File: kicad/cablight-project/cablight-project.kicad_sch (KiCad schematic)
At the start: 16 parts, among them J1 Screw_Term_1x2_2.54mm, J2 Screw_Term_1x2_2.54mm, P1 Pololu D24V10F5, Q1 IRLB8721PBF, SW1 PEC11, SW3 switch_SPDT_SLW_121586

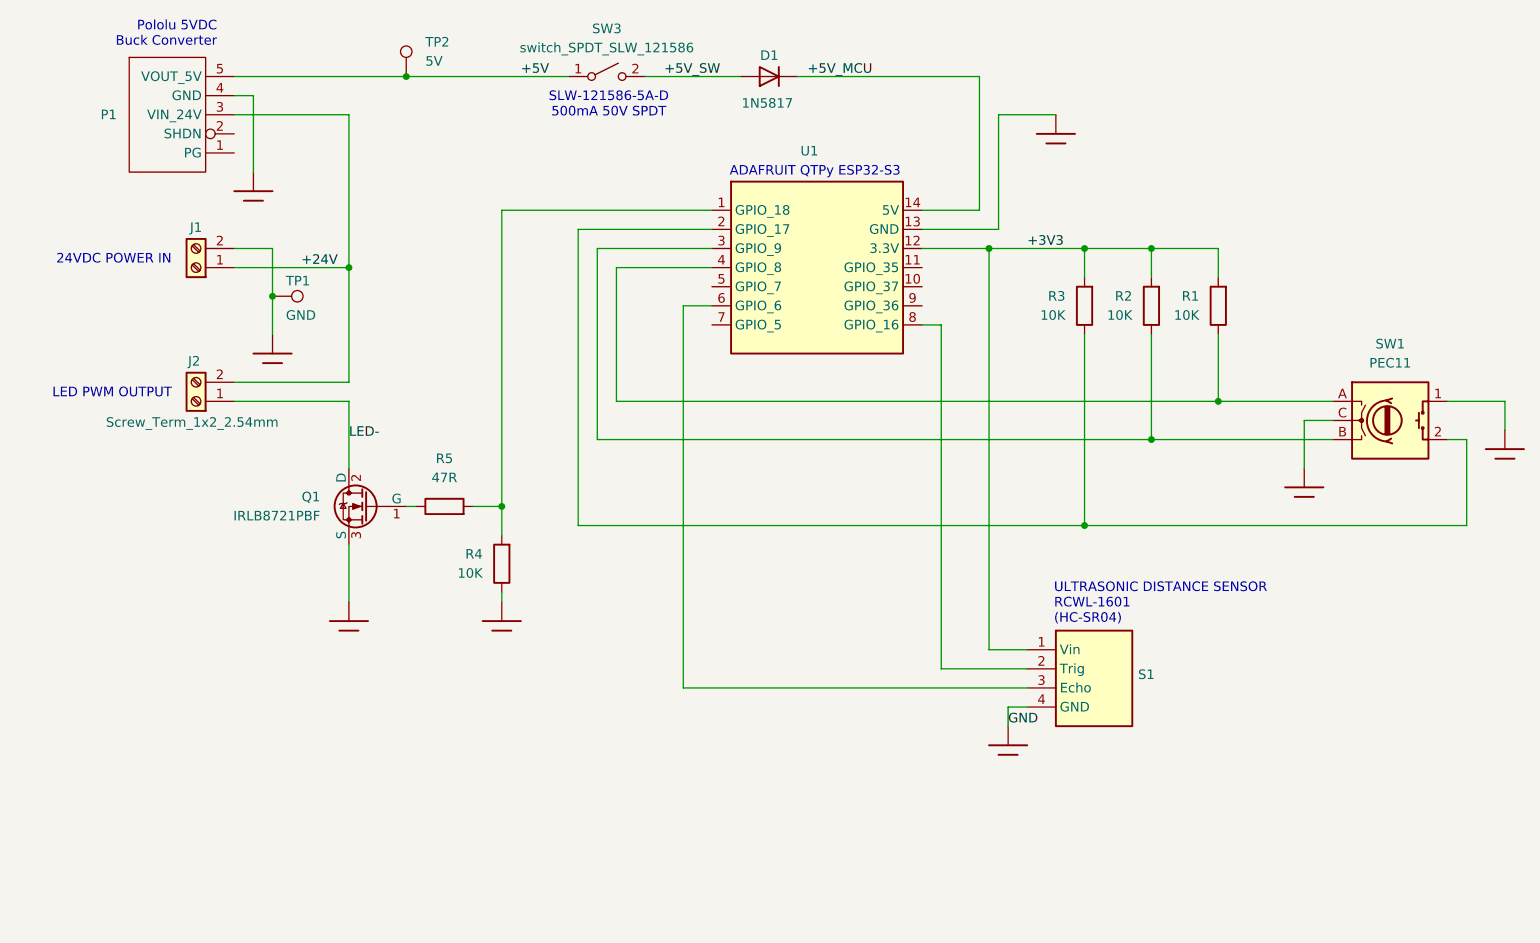
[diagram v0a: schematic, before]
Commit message: Add Button code support and make ultrasonic notify from task.
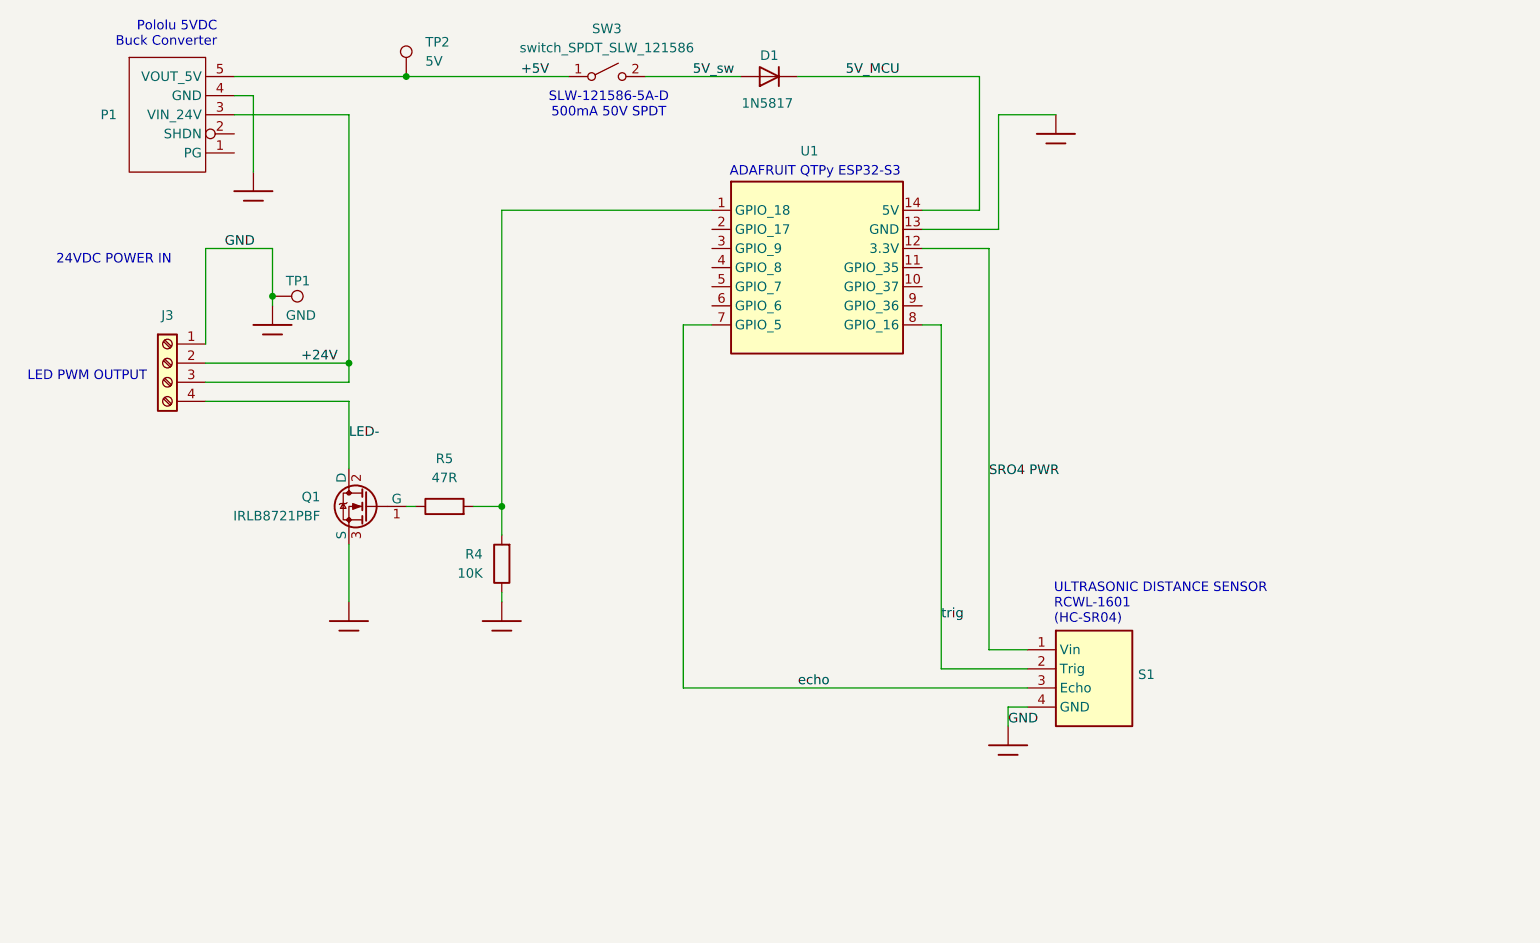
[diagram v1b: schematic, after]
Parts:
- removed J1, J2: Screw_Term_1x2_2.54mm, user:2xTermBlock_254mm, symbol user:Screw_Term_1x2_2.54mm
- removed R1, R2, R3: 10K, Resistor_THT:R_Axial_DIN0207_L6.3mm_D2.5mm_P10.16mm_Horizontal, symbol user:R
- removed SW1: PEC11, user:Bourns-PEC11R, symbol Device:RotaryEncoder_Switch
- added J3: Screw_Term_1x4_5mm, Library:Molex 4pin Terminal Block, symbol extra:Screw_Term_1x4_5mm
- R4, R5: footprint Resistor_THT:R_Axial_DIN0207_L6.3mm_D2.5mm_P10.16mm_Horizontal -> Resistor_THT:R_Axial_DIN0207_L6.3mm_D2.5mm_P9.5mm
- TP1, TP2: footprint TestPoint:TestPoint_Plated_Hole_D2.0mm -> TestPoint:TestPoint_THTPad_D1.0mm_Drill0.5mm
- U1: footprint user:AdafruitQTPyEsp32S3 -> GRK_Lib:AdafruitQTPyEsp32S3; symbol user:Adafruit_QTPy_Esp32S3 -> GRK_Global_Sym_Lib:Adafruit_QTPy_Esp32S3
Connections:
- net +24V: now also J3.2 (Pin_2), J3.3 (Pin_3)
- net GND: now also TP1.1, J3.1 (Pin_1)
- net LED-: now also J3.4 (Pin_4)
- net at U1.6 (GPIO_6): no longer S1.3 (Echo)
- net echo: now reaches U1.7 (GPIO_5)
- net echo: now also S1.3 (Echo)
- net trig: now reaches S1.2 (Trig), U1.8 (GPIO_16)
- net +3V3 renamed SRO4 PWR
- net +5V_MCU renamed 5V_MCU
- net +5V_SW renamed 5V_sw

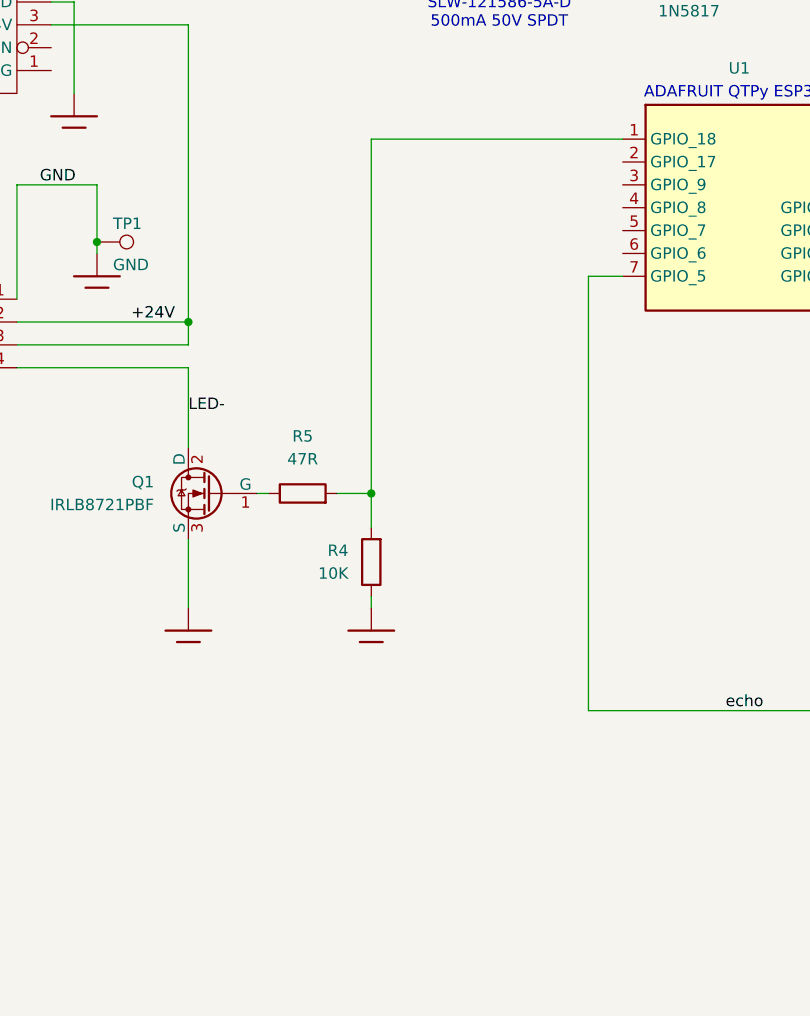
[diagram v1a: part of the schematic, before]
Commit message: add DIP switch to kicad
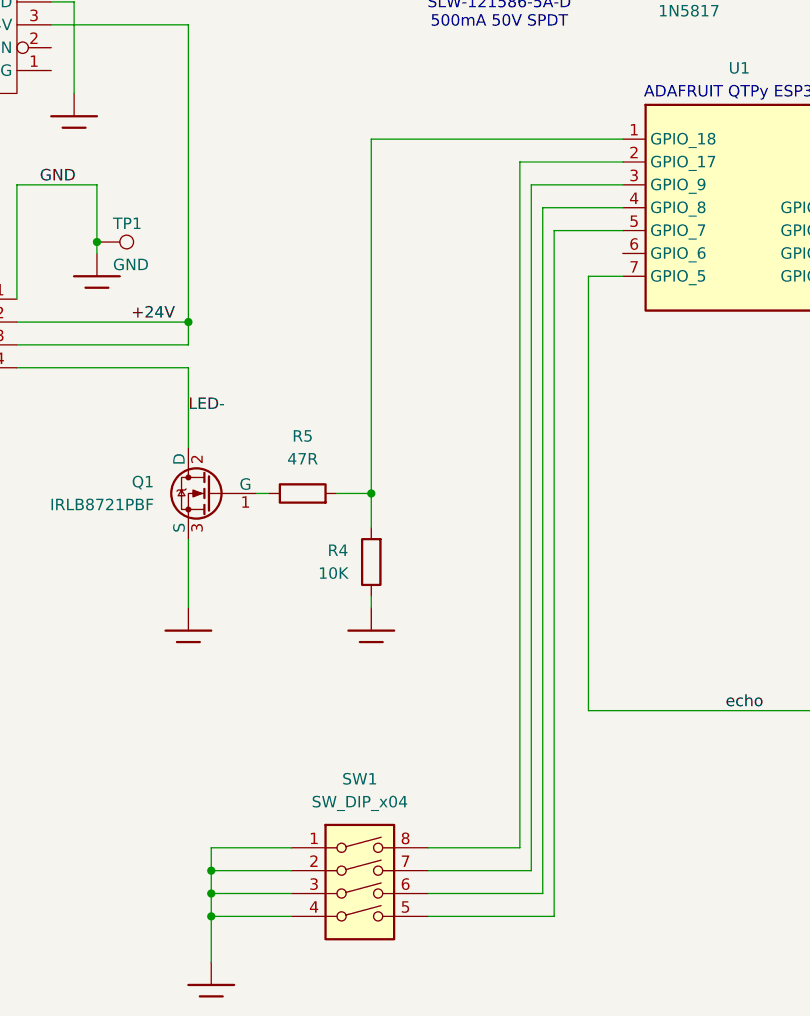
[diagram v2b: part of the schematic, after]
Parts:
- added SW1: SW_DIP_x04, GRK_Lib:DIP-4 DS04-254 SAME SKY, symbol Switch:SW_DIP_x04
- J3: footprint Library:Molex 4pin Terminal Block -> GRK_Lib:Molex 4pin Terminal Block
- P1: footprint user:Pololu_5V_H -> GRK_Lib:Pololu_5V_H
- Q1: footprint user:TO-220F-3_H_Heatsink -> GRK_Lib:TO-220F-3_H_Heatsink
- S1: footprint user:RCWL-1601 -> GRK_Lib:RCWL-1601
- SW3: footprint user:CUI_SPDT_500mA_3mm -> GRK_Lib:Switch_SPDT_CUI_500mA_3mm
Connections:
- net at U1.2 (GPIO_17): now also SW1.8
- net at U1.3 (GPIO_9): now also SW1.7
- net at U1.4 (GPIO_8): now also SW1.6
- net at U1.5 (GPIO_7): now also SW1.5
- new net: SW1.1, SW1.2, SW1.3, SW1.4

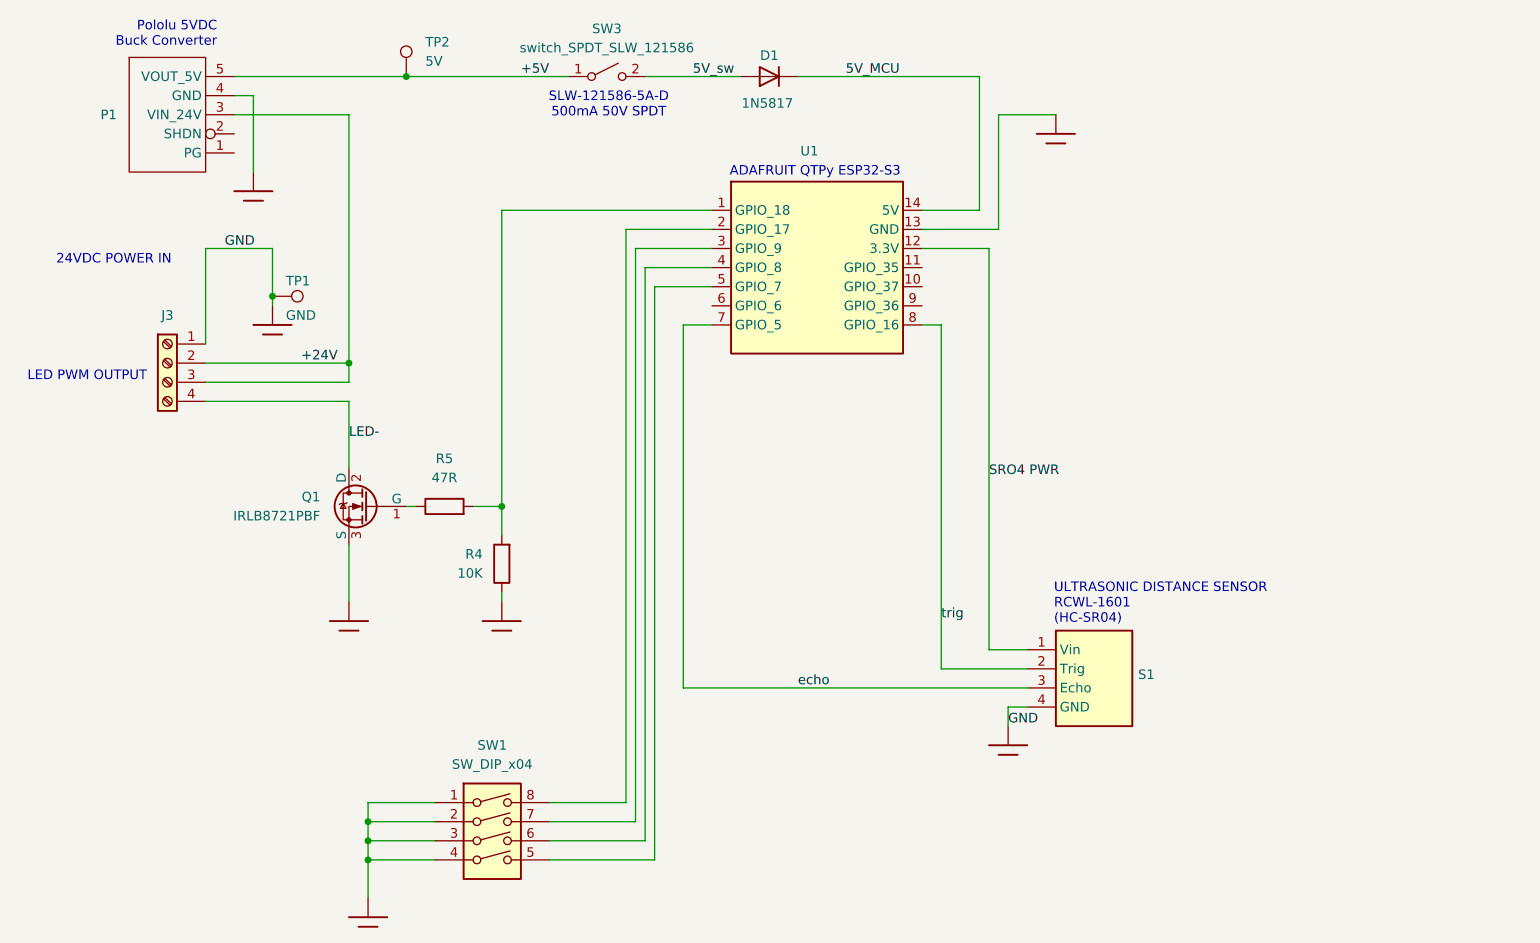
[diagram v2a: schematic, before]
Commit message: Layout KiCAD for DIP switches and button.
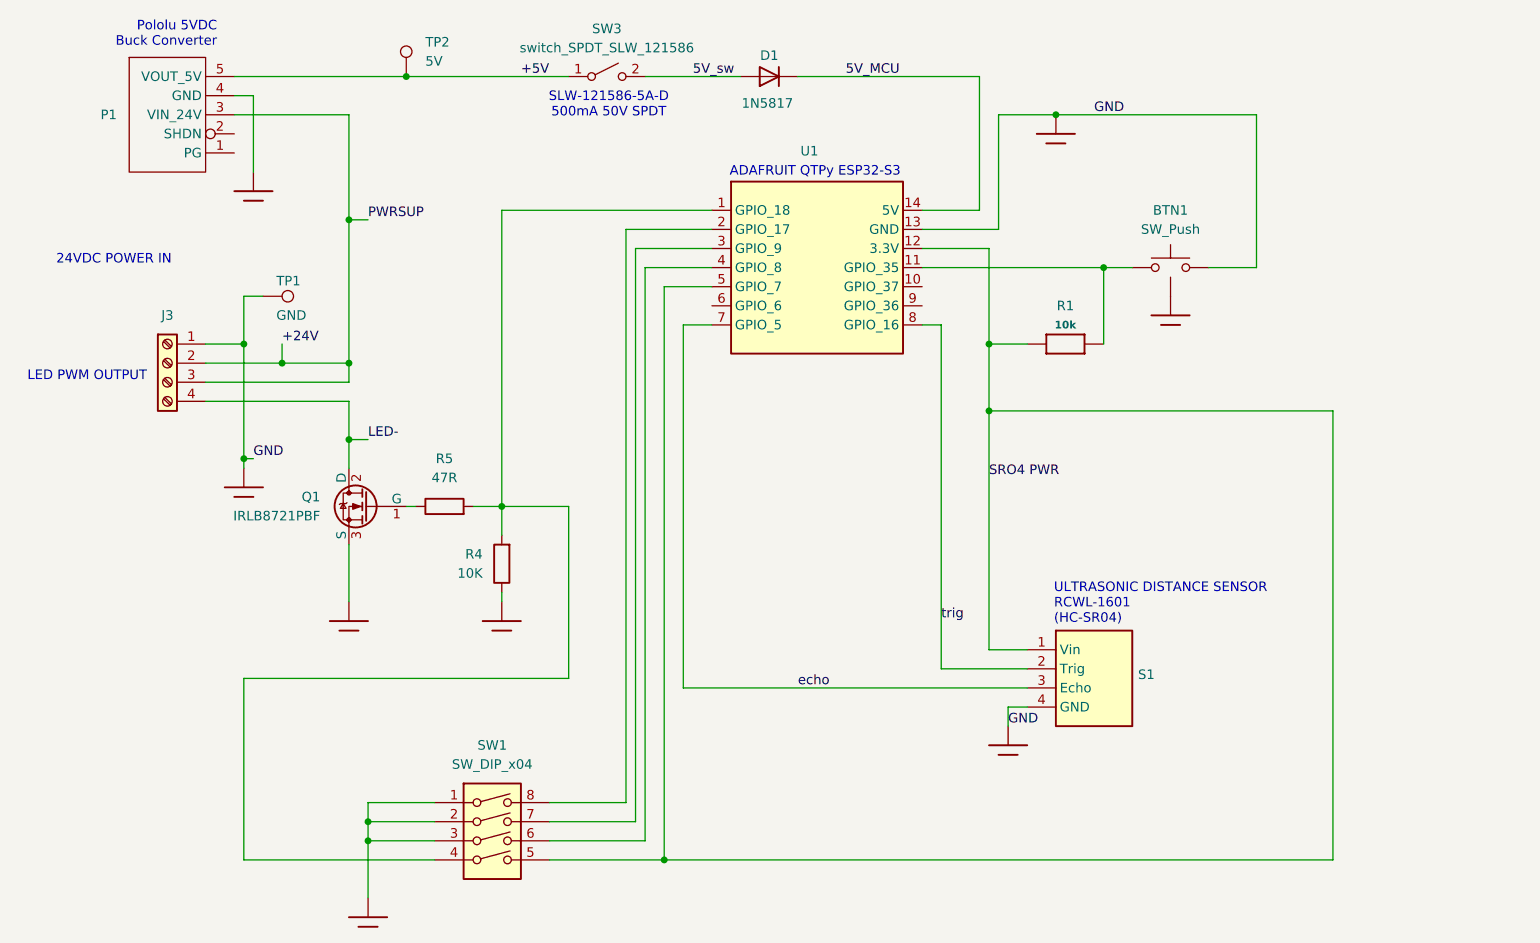
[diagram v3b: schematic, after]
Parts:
- added BTN1: SW_Push, GRK_Lib:Tactile Switch Wurth, symbol GRK_Global_Sym_Lib:SW_Push_With_GND
- added R1: 10k, Resistor_SMD:R_0805_2012Metric_Pad1.20x1.40mm_HandSolder, symbol cablight-eagle-import:RESISTOR_0805
- R4, R5: footprint Resistor_THT:R_Axial_DIN0207_L6.3mm_D2.5mm_P9.5mm -> Resistor_SMD:R_0805_2012Metric_Pad1.20x1.40mm_HandSolder
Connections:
- net GND: now also U1.13 (GND), BTN1.2
- net SRO4 PWR: now also SW1.5, U1.5 (GPIO_7), R1.1
- net at R4.1, R5.1, U1.1 (GPIO_18): now also SW1.4
- net at U1.11 (GPIO_35): now also BTN1.1, R1.2
- net at SW1.1, SW1.2, SW1.3: no longer SW1.4
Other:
- moved on the sheet: TP1

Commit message: progress
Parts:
- S1: footprint GRK_Lib:RCWL-1601 -> GRK_Lib:Molex 4pin Terminal Block 2.54mm
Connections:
- net at U1.10 (GPIO_37): now also U1.6 (GPIO_6), U1.9 (GPIO_36)
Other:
- note added: "Grounding all un-used pins."
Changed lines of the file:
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@@
+		)
+	)
+	(text "Grounding all\nun-used pins."
+		(exclude_from_sim no)
+		(at 131.064 101.092 0)
+		(effects
+			(font
+				(size 1.27 1.27)
+			)
 		)
 	)
@@
 	)
 	(junction
+		(at 149.86 77.47)
+		(diameter 0)
+		(color 0 0 0 0)
+	)
+	(junction
 		(at 162.56 52.07)
 		(diameter 0)
@@
 	)
 	(junction
+		(at 130.81 92.71)
+		(diameter 0)
+		(color 0 0 0 0)
+	)
+	(junction
 		(at 153.67 82.55)
 		(diameter 0)
@@
 	(wire
 		(pts
+			(xy 149.86 77.47) (xy 149.86 92.71)
+		)
+		(stroke
+			(width 0)
+			(type default)
+		)
+	)
+	(wire
+		(pts
+			(xy 149.86 74.93) (xy 149.86 77.47)
+		)
+		(stroke
+			(width 0)
+			(type default)
+		)
+	)
+	(wire
+		(pts
 			(xy 54.61 76.2) (xy 57.15 76.2)
 		)
@@
 	(wire
 		(pts
+			(xy 149.86 92.71) (xy 130.81 92.71)
+		)
+		(stroke
+			(width 0)
+			(type default)
+		)
+	)
+	(wire
+		(pts
 			(xy 77.47 104.14) (xy 76.2 104.14)
 		)
@@
 	(wire
 		(pts
+			(xy 144.78 74.93) (xy 149.86 74.93)
+		)
+		(stroke
+			(width 0)
+			(type default)
+		)
+	)
+	(wire
+		(pts
+			(xy 116.84 77.47) (xy 114.3 77.47)
+		)
+		(stroke
+			(width 0)
+			(type default)
+		)
+	)
+	(wire
+		(pts
 			(xy 71.12 146.05) (xy 71.12 148.59)
 		)
@@
 	(wire
 		(pts
+			(xy 144.78 77.47) (xy 149.86 77.47)
+		)
+		(stroke
+			(width 0)
+			(type default)
+		)
+	)
+	(wire
+		(pts
 			(xy 116.84 69.85) (xy 106.68 69.85)
 		)
@@
 	(wire
 		(pts
+			(xy 114.3 92.71) (xy 130.81 92.71)
+		)
+		(stroke
+			(width 0)
+			(type default)
+		)
+	)
+	(wire
+		(pts
 			(xy 80.01 143.51) (xy 71.12 143.51)
 		)
@@
 		(pts
 			(xy 68.58 90.17) (xy 68.58 95.25)
+		)
+		(stroke
+			(width 0)
+			(type default)
+		)
+	)
+	(wire
+		(pts
+			(xy 114.3 77.47) (xy 114.3 92.71)
 		)
 		(stroke
@@
 				(path "/2aa36568-293b-470b-bbef-a9ff44d0879c"
 					(reference "U1")
+					(unit 1)
+				)
+			)
+		)
+	)
+	(symbol
+		(lib_id "user:GND")
+		(at 130.81 95.25 0)
+		(mirror y)
+		(unit 1)
+		(exclude_from_sim no)
+		(in_bom yes)
+		(on_board yes)
+		(dnp no)
+		(fields_autoplaced yes)
+		(property "Reference" "#07"
+			(at 130.81 95.25 0)
+			(effects
+				(font
+					(size 1.27 1.27)
+				)
+				(hide yes)
+			)
+		)
+		(property "Value" "~"
+			(at 130.81 97.79 0)
+			(effects
+				(font
+					(size 1.27 1.0795)
+				)
+			)
+		)
+		(property "Footprint" ""
+			(at 132.08 95.25 0)
+			(effects
+				(font
+					(size 1.27 1.27)
+				)
+				(hide yes)
+			)
+		)
+		(property "Datasheet" ""
+			(at 132.08 95.25 0)
+			(effects
+				(font
+					(size 1.27 1.27)
+				)
+				(hide yes)
+			)
+		)
+		(property "Description" "GND"
+			(at 130.81 95.25 0)
+			(effects
+				(font
+					(size 1.27 1.27)
+				)
+				(hide yes)
+			)
+		)
+		(pin "1"
+		)
+		(instances
+			(project "cablight-project"
+				(path "/2aa36568-293b-470b-bbef-a9ff44d0879c"
+					(reference "#07")
 					(unit 1)
 				)
@@
 			)
 		)
-		(property "Footprint" "GRK_Lib:RCWL-1601"
+		(property "Footprint" "GRK_Lib:Molex 4pin Terminal Block 2.54mm"
 			(at 165.1 137.16 0)
 			(effects

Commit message: progress
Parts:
- S1: footprint GRK_Lib:Molex 4pin Terminal Block 2.54mm -> GRK_Lib:JST 4-Pin 2mm Pitch Vertical
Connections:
- net trig: no longer S1.2 (Trig), U1.8 (GPIO_16)
- net at U1.10 (GPIO_37), U1.9 (GPIO_36): now also U1.8 (GPIO_16); no longer U1.6 (GPIO_6)
- new net: S1.2 (Trig), U1.6 (GPIO_6)
